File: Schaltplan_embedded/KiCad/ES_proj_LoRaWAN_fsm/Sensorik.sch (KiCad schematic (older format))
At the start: 22 parts

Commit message: Schaltung_Keramik_Antenne
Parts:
- added C?: 1uF, symbol Device:C
- added C?: 2.2uF, symbol Device:C
- added IC?: TPS22943DCKR, SOT65P210X110-5N, symbol SamacSys_Parts:TPS22943DCKR
- added R? (x7): 0, symbol Device:R
- added R? (x2): NM, symbol Device:R
- added R?: 100k, symbol Device:R
- added R?: 10k, symbol Device:R
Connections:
- net 3V3: no longer C?.2, IC?.2 (VCC), IC?.6 (PON)
- net GND: now also C?.2, C?.2, IC?.2 (GND), R?.1
- net at C?.1, L?.2: now also R?.2
- new net: C?.1, IC?.1 (VOUT), R?.1
- new net: C?.1, IC?.5 (VIN), R?.1, R?.1, R?.2, R?.2
- new net: IC?.3 (OC), R?.2
- new net: IC?.4 (ON), R?.1, R?.2
- new net: C?.2, IC?.2 (VCC), R?.1
- new net: IC?.6 (PON), R?.1, R?.2
- new net AntOFF: R?.1, R?.2, R?.2
- new net VCC_RF: R?.1, R?.1, R?.2, R?.2
- new net Vant: R?.1, R?.2
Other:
- moved on the sheet: C?, J?, U?

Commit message: Neuer Schaltplan
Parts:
- removed R? (x7): 0, symbol Device:R
- removed R? (x2): NM, symbol Device:R
- C25, C26, C27, C28: renamed from C?; footprint (none) -> Capacitors_SMD:C_0805_HandSoldering
- C29, C30, C31, C32, C33, C34, C35, C36, C37: renamed from C?; footprint (none) -> Capacitors_SMD:C_0805
- D3: renamed from D?; footprint ESDARF021BU2CK -> (none)
- IC5: renamed from IC?; footprint SOT65P210X110-5N -> (none)
- IC6: renamed from IC?; footprint BGS12SN6E6327XTSA1 -> (none)
- IC7: renamed from IC?; footprint SON110P970X1010X230-18N -> (none)
- gave numbers to parts that had none: 10
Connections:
- net 3V3 is gone; now on net +3V3: C25.2, C26.2, C30.1, L4.1, U2.13 (3.3V)
- net AntOFF: now also IC5.4 (ON), IC6.6 (PON)
- net at C31.1, IC5.1 (VOUT): now also C27.1, L2.2
- net +3V3: now reaches C36.1, IC5.5 (VIN), R21.1
- net +3V3: now also C35.2, IC6.2 (VCC)
- net 5V renamed +5V

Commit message: Bauteilliste vollständig und Schaltplan entsprechend geändert
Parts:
- removed J4, J6: Conn_Coaxial, symbol Connector:Conn_Coaxial
- added J4, J6: 73100-0258, SamacSys_Parts:731000258, symbol SamacSys_Parts:73100-0258
- D3: footprint (none) -> SamacSys_Parts:ESDARF021BU2CK
- FL1: footprint (none) -> SamacSys_Parts:B39162B4353P810
- IC5: footprint (none) -> SamacSys_Parts:SOT65P210X110-5N
- IC6: footprint (none) -> SamacSys_Parts:BGA725L6E6327
- IC7: footprint (none) -> SamacSys_Parts:SON110P970X1010X230-18N
- J5: footprint (none) -> Pin_Headers:Pin_Header_Straight_1x08_Pitch1.00mm
- L2, L3, L4, R17, R21: footprint (none) -> Resistors_SMD:R_0805_HandSoldering
- U2: footprint (none) -> RF_Modules:Hopref_RFM9XW_SMD
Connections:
- net GND: now also J4.1, J4.2, J4.3, J4.4, J6.1, J6.2, J6.3, J6.4
- net at C28.2, D3.1, L2.1: now also J6.5
- net at U2.9 (ANT): now also J4.5
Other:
- moved on the sheet: C25, C26, R17, U2

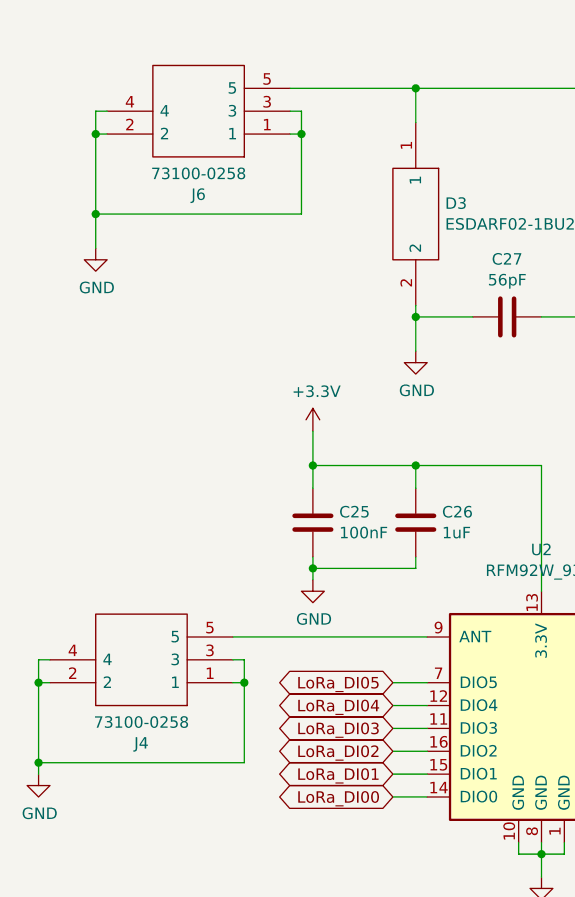
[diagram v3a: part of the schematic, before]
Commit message: Schaltplanänderung
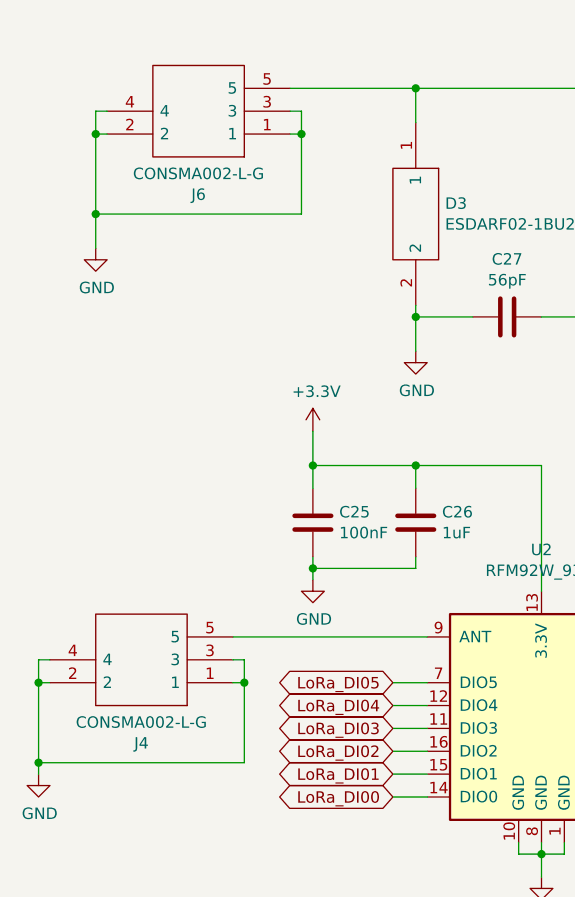
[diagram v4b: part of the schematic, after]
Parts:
- removed J4, J6: 73100-0258, SamacSys_Parts:731000258, symbol SamacSys_Parts:73100-0258
- added J4, J6: CONSMA002-L-G, SamacSys_Parts:CONSMA002LG, symbol SamacSys_Parts:CONSMA002-L-G
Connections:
- net GND: now also J4.1, J4.2, J4.3, J4.4, J6.1, J6.2, J6.3, J6.4
- net at C28.2, D3.1, L2.1: now also J6.5
- net at U2.9 (ANT): now also J4.5
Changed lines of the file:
@@
 Wire Wire Line
 	8950 3050 8950 5500
-$Comp
-L SamacSys_Parts:73100-0258 J4
-U 1 1 5DE081B6
-P 1500 6650
-F 0 "J4" H 1900 6915 50  0000 C CNN
-F 1 "73100-0258" H 1900 6824 50  0000 C CNN
-F 2 "SamacSys_Parts:731000258" H 2150 6750 50  0001 L CNN
-F 3 "https://componentsearchengine.com/Datasheets/1/73100-0258.pdf" H 2150 6650 50  0001 L CNN
-F 4 "MOLEX - 73100-0258 - RF COAX CONN, SMB, JACK, 75 OHM, PCB" H 2150 6550 50  0001 L CNN "Description"
-F 5 "7.49" H 2150 6450 50  0001 L CNN "Height"
-F 6 "538-73100-0258" H 2150 6350 50  0001 L CNN "Mouser Part Number"
-F 7 "https://www.mouser.com/Search/Refine.aspx?Keyword=538-73100-0258" H 2150 6250 50  0001 L CNN "Mouser Price/Stock"
-F 8 "Molex" H 2150 6150 50  0001 L CNN "Manufacturer_Name"
-F 9 "73100-0258" H 2150 6050 50  0001 L CNN "Manufacturer_Part_Number"
-	1    1500 6650
-	-1   0    0    1
-$EndComp
 Wire Wire Line
 	1500 6450 2350 6450
@@
 Wire Wire Line
 	1550 6650 1550 7000
-$Comp
-L SamacSys_Parts:73100-0258 J6
-U 1 1 5DE559F1
-P 1750 4250
-F 0 "J6" H 2150 4515 50  0000 C CNN
-F 1 "73100-0258" H 2150 4424 50  0000 C CNN
-F 2 "SamacSys_Parts:731000258" H 2400 4350 50  0001 L CNN
-F 3 "https://componentsearchengine.com/Datasheets/1/73100-0258.pdf" H 2400 4250 50  0001 L CNN
-F 4 "MOLEX - 73100-0258 - RF COAX CONN, SMB, JACK, 75 OHM, PCB" H 2400 4150 50  0001 L CNN "Description"
-F 5 "7.49" H 2400 4050 50  0001 L CNN "Height"
-F 6 "538-73100-0258" H 2400 3950 50  0001 L CNN "Mouser Part Number"
-F 7 "https://www.mouser.com/Search/Refine.aspx?Keyword=538-73100-0258" H 2400 3850 50  0001 L CNN "Mouser Price/Stock"
-F 8 "Molex" H 2400 3750 50  0001 L CNN "Manufacturer_Name"
-F 9 "73100-0258" H 2400 3650 50  0001 L CNN "Manufacturer_Part_Number"
-	1    1750 4250
-	-1   0    0    1
-$EndComp
 Wire Wire Line
 	1750 4050 2300 4050
@@
 Wire Wire Line
 	1800 4250 1800 4600
+$Comp
+L SamacSys_Parts:CONSMA002-L-G J6
+U 1 1 5DDFF1AD
+P 1750 4250
+F 0 "J6" H 2150 4515 50  0000 C CNN
+F 1 "CONSMA002-L-G" H 2150 4424 50  0000 C CNN
+F 2 "SamacSys_Parts:CONSMA002LG" H 2400 4350 50  0001 L CNN
+F 3 "https://componentsearchengine.com/Datasheets/1/CONSMA002-L-G.pdf" H 2400 4250 50  0001 L CNN
+F 4 "RF Connectors / Coaxial Connectors SMA Fml Right Angle PCB Mount, Extended" H 2400 4150 50  0001 L CNN "Description"
+F 5 "10" H 2400 4050 50  0001 L CNN "Height"
+F 6 "712-CONSMA002-L-G" H 2400 3950 50  0001 L CNN "Mouser Part Number"
+F 7 "https://www.mouser.com/Search/Refine.aspx?Keyword=712-CONSMA002-L-G" H 2400 3850 50  0001 L CNN "Mouser Price/Stock"
+F 8 "Linx Technologies" H 2400 3750 50  0001 L CNN "Manufacturer_Name"
+F 9 "CONSMA002-L-G" H 2400 3650 50  0001 L CNN "Manufacturer_Part_Number"
+	1    1750 4250
+	-1   0    0    1
+$EndComp
+$Comp
+L SamacSys_Parts:CONSMA002-L-G J4
+U 1 1 5DE088FB
+P 1500 6650
+F 0 "J4" H 1900 6915 50  0000 C CNN
+F 1 "CONSMA002-L-G" H 1900 6824 50  0000 C CNN
+F 2 "SamacSys_Parts:CONSMA002LG" H 2150 6750 50  0001 L CNN
+F 3 "https://componentsearchengine.com/Datasheets/1/CONSMA002-L-G.pdf" H 2150 6650 50  0001 L CNN
+F 4 "RF Connectors / Coaxial Connectors SMA Fml Right Angle PCB Mount, Extended" H 2150 6550 50  0001 L CNN "Description"
+F 5 "10" H 2150 6450 50  0001 L CNN "Height"
+F 6 "712-CONSMA002-L-G" H 2150 6350 50  0001 L CNN "Mouser Part Number"
+F 7 "https://www.mouser.com/Search/Refine.aspx?Keyword=712-CONSMA002-L-G" H 2150 6250 50  0001 L CNN "Mouser Price/Stock"
+F 8 "Linx Technologies" H 2150 6150 50  0001 L CNN "Manufacturer_Name"
+F 9 "CONSMA002-L-G" H 2150 6050 50  0001 L CNN "Manufacturer_Part_Number"
+	1    1500 6650
+	-1   0    0    1
+$EndComp
 $EndSCHEMATC
